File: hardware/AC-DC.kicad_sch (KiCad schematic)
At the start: 9 parts, among them J8 Conn_01x02

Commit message: custom fuse footprint with 3d model
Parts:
- F1: footprint Fuse:Fuse_Bourns_MF-RG300 -> ProjectLibrary:Fuse
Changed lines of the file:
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@@
       (effects (font (size 1.27 1.27)))
     )
-    (property "Footprint" "Fuse:Fuse_Bourns_MF-RG300" (at 35.56 28.448 90)
+    (property "Footprint" "ProjectLibrary:Fuse" (at 35.56 28.448 90)
       (effects (font (size 1.27 1.27)) hide)
     )

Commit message: change tantalum capacitor to ceramic
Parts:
- C2: value 100uF -> 47uF; footprint Capacitor_Tantalum_SMD:CP_EIA-3528-21_Kemet-B -> Capacitor_SMD:C_1206_3216Metric; JLCPCB Part # C16133 -> C96123
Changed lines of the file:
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@@
       (effects (font (size 1.27 1.27)) (justify left))
     )
-    (property "Value" "100uF" (at 125.73 34.29 0)
+    (property "Value" "47uF" (at 125.73 34.29 0)
       (effects (font (size 1.27 1.27)) (justify left))
     )
-    (property "Footprint" "Capacitor_Tantalum_SMD:CP_EIA-3528-21_Kemet-B" (at 124.46 31.75 0)
+    (property "Footprint" "Capacitor_SMD:C_1206_3216Metric" (at 124.46 31.75 0)
       (effects (font (size 1.27 1.27)) hide)
     )
@@
       (effects (font (size 1.27 1.27)) hide)
     )
-    (property "JLCPCB Part #" "C16133" (at 124.46 31.75 0)
+    (property "JLCPCB Part #" "C96123" (at 124.46 31.75 0)
       (effects (font (size 1.27 1.27)) hide)
     )

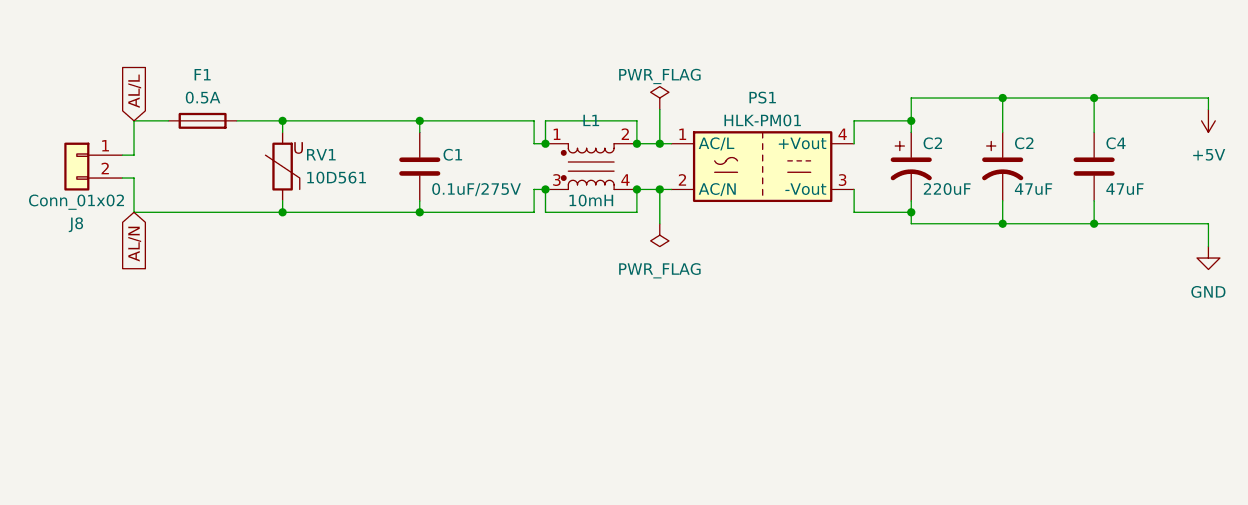
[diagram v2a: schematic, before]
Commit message: 5V/GND connector
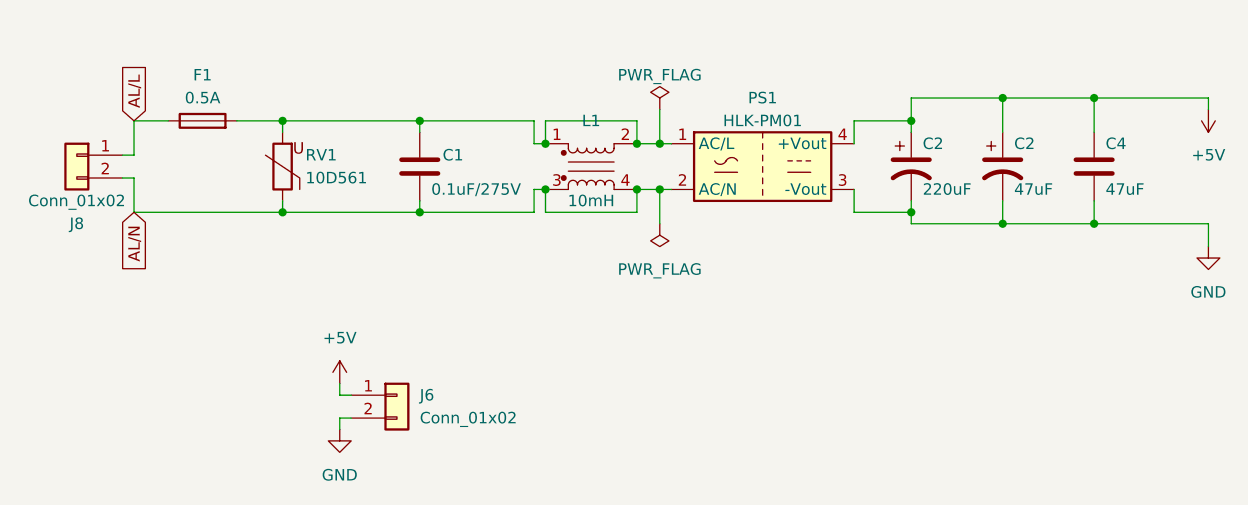
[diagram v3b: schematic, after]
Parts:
- added J6: Conn_01x02, Connector_PinHeader_2.54mm:PinHeader_1x02_P2.54mm_Vertical, symbol Connector_Generic:Conn_01x02
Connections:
- net +5V: now also J6.1 (Pin_1)
- net GND: now also J6.2 (Pin_2)
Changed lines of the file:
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@@
+    (stroke (width 0) (type default))
+  )
+  (wire (pts (xy 50.8 55.88) (xy 50.8 57.15))
     (stroke (width 0) (type default))
   )
@@
     (stroke (width 0) (type default))
   )
+  (wire (pts (xy 50.8 57.15) (xy 52.07 57.15))
+    (stroke (width 0) (type default))
+  )
   (wire (pts (xy 147.32 38.1) (xy 134.62 38.1))
     (stroke (width 0) (type default))
@@
     (stroke (width 0) (type default))
   )
+  (wire (pts (xy 50.8 59.69) (xy 52.07 59.69))
+    (stroke (width 0) (type default))
+  )
   (wire (pts (xy 114.3 26.67) (xy 107.95 26.67))
     (stroke (width 0) (type default))
@@
   )
   (wire (pts (xy 72.39 34.29) (xy 72.39 36.83))
+    (stroke (width 0) (type default))
+  )
+  (wire (pts (xy 50.8 60.96) (xy 50.8 59.69))
     (stroke (width 0) (type default))
   )
@@
     )
   )
+  (symbol (lib_id "power:GND") (at 50.8 60.96 0) (unit 1)
+    (in_bom yes) (on_board yes) (dnp no) (fields_autoplaced)
+    (property "Reference" "#PWR0103" (at 50.8 67.31 0)
+      (effects (font (size 1.27 1.27)) hide)
+    )
+    (property "Value" "GND" (at 50.8 66.04 0)
+      (effects (font (size 1.27 1.27)))
+    )
+    (property "Footprint" "" (at 50.8 60.96 0)
+      (effects (font (size 1.27 1.27)) hide)
+    )
+    (property "Datasheet" "" (at 50.8 60.96 0)
+      (effects (font (size 1.27 1.27)) hide)
+    )
+    (pin "1")
+    (instances
+      (project "AquariumController"
+        (path "/75069d71-4fd1-4b49-820b-d8e60608591a"
+          (reference "#PWR0103") (unit 1)
+        )
+        (path "/75069d71-4fd1-4b49-820b-d8e60608591a/cae2cbae-b73f-4926-bf8f-e52abe478c81"
+          (reference "#PWR017") (unit 1)
+        )
+      )
+      (project "XIAO-ESP32C3-aquarium-controller"
+        (path "/e16639bd-7ef7-40a4-9337-f1b4c79f775b/bee5e875-31e5-4be6-8420-aaa58bd7d71a"
+          (reference "#PWR039") (unit 1)
+        )
+      )
+    )
+  )
+  (symbol (lib_id "Connector_Generic:Conn_01x02") (at 57.15 57.15 0) (unit 1)
+    (in_bom yes) (on_board yes) (dnp no) (fields_autoplaced)
+    (property "Reference" "J6" (at 59.69 57.15 0)
+      (effects (font (size 1.27 1.27)) (justify left))
+    )
+    (property "Value" "Conn_01x02" (at 59.69 59.69 0)
+      (effects (font (size 1.27 1.27)) (justify left))
+    )
+    (property "Footprint" "Connector_PinHeader_2.54mm:PinHeader_1x02_P2.54mm_Vertical" (at 57.15 57.15 0)
+      (effects (font (size 1.27 1.27)) hide)
+    )
+    (property "Datasheet" "~" (at 57.15 57.15 0)
+      (effects (font (size 1.27 1.27)) hide)
+    )
+    (pin "1")
+    (pin "2")
+    (instances
+      (project "XIAO-ESP32C3-aquarium-controller"
+        (path "/e16639bd-7ef7-40a4-9337-f1b4c79f775b/bee5e875-31e5-4be6-8420-aaa58bd7d71a"
+          (reference "J6") (unit 1)
+        )
+      )
+    )
+  )
   (symbol (lib_id "Device:Varistor") (at 44.45 31.75 180) (unit 1)
     (in_bom no) (on_board yes) (dnp no)
@@
         )
       )
+    )
+  )
+  (symbol (lib_id "power:+5V") (at 50.8 55.88 0) (unit 1)
+    (in_bom yes) (on_board yes) (dnp no) (fields_autoplaced)
+    (property "Reference" "#PWR0102" (at 50.8 59.69 0)
+      (effects (font (size 1.27 1.27)) hide)
+    )
+    (property "Value" "+5V" (at 50.8 50.8 0)
+      (effects (font (size 1.27 1.27)))
+    )
+    (property "Footprint" "" (at 50.8 55.88 0)
+      (effects (font (size 1.27 1.27)) hide)
+    )
+    (property "Datasheet" "" (at 50.8 55.88 0)
+      (effects (font (size 1.27 1.27)) hide)
+    )
+    (pin "1")
+    (instances
+      (project "AquariumController"
+        (path "/75069d71-4fd1-4b49-820b-d8e60608591a"
+          (reference "#PWR0102") (unit 1)
+        )
+        (path "/75069d71-4fd1-4b49-820b-d8e60608591a/cae2cbae-b73f-4926-bf8f-e52abe478c81"
+          (reference "#PWR016") (unit 1)
+        )
+      )
+      (project "XIAO-ESP32C3-aquarium-controller"
+        (path "/e16639bd-7ef7-40a4-9337-f1b4c79f775b/bee5e875-31e5-4be6-8420-aaa58bd7d71a"
+          (reference "#PWR040") (unit 1)
+        )
+      )

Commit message: some bom exclusions, jlcpcb rotations
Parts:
- J6: now left out of the parts list
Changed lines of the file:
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@@
   )
   (symbol (lib_id "Connector_Generic:Conn_01x02") (at 57.15 57.15 0) (unit 1)
-    (in_bom yes) (on_board yes) (dnp no) (fields_autoplaced)
+    (in_bom no) (on_board yes) (dnp no) (fields_autoplaced)
     (property "Reference" "J6" (at 59.69 57.15 0)
       (effects (font (size 1.27 1.27)) (justify left))

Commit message: labeling
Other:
- note added: "High Voltage"
- title: (none) -> AC to DC
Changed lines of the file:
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@@
 (kicad_sch (version 20230121) (generator eeschema)
   (paper "A4")
+  (title_block
+    (title "AC to DC")
+  )
   (junction (at 114.3 36.83) (diameter 0) (color 0 0 0 0)
   )
@@
     (stroke (width 0) (type default))
   )
+  (rectangle (start 15.24 15.24) (end 99.06 46.99)
+    (stroke (width 0) (type default))
+    (fill (type none))
+  )
+  (text "High Voltage" (at 52.07 19.05 0)
+    (effects (font (size 1.27 1.27)) (justify left bottom))
+  )
   (global_label "AL{slash}N" (shape input) (at 27.94 36.83 270) (fields_autoplaced)
